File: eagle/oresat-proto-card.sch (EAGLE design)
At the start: 61 parts, among them J1 J-SAMTEC-TFM-110-X1-XXX-D-RA, J2 U.FL, J3 U.FL, J4 U.FL, J6 J-SAMTEC-TFM-120-X1-XXX-D-RA, J7 1.27MM-SWD-CONNECTOR, U1 TPS63070, U2 TCAN330, U6 STM32F042K6, X1 16MHZ-2.5x2mm

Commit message: Added some attributes.
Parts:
- J1: DIS (none) -> Digi-Key; DPN (none) -> SAM10113-ND; MFR (none) -> Samtec; MPN (none) -> TFM-110-01-L-D-RA
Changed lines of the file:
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@@
 <part name="JP8" library="pinhead" library_urn="urn:adsk.eagle:library:325" deviceset="PINHD-1X2" device="" package3d_urn="urn:adsk.eagle:package:22435/2"/>
 <part name="VBUS2" library="oresat-supplies" deviceset="VBUS" device=""/>
-<part name="J1" library="J-Samtec-TFM-110-X1-XXX-D-RA" deviceset="J-SAMTEC-TFM-110-X1-XXX-D-RA" device=""/>
+<part name="J1" library="J-Samtec-TFM-110-X1-XXX-D-RA" deviceset="J-SAMTEC-TFM-110-X1-XXX-D-RA" device="">
+<attribute name="DIS" value="Digi-Key"/>
+<attribute name="DPN" value="SAM10113-ND"/>
+<attribute name="MFR" value="Samtec"/>
+<attribute name="MPN" value="TFM-110-01-L-D-RA "/>
+</part>
 <part name="JP9" library="pinhead" library_urn="urn:adsk.eagle:library:325" deviceset="PINHD-1X10" device="" package3d_urn="urn:adsk.eagle:package:22406/2"/>
 <part name="JP10" library="pinhead" library_urn="urn:adsk.eagle:library:325" deviceset="PINHD-2X5" device="" package3d_urn="urn:adsk.eagle:package:22470/2"/>
@@
 <attribute name="NAME" x="22.86" y="83.185" size="1.778" layer="95" rot="MR0"/>
 <attribute name="VALUE" x="10.16" y="25.4" size="1.778" layer="96"/>
+<attribute name="DIS" x="16.51" y="57.15" size="1.778" layer="96" rot="MR0" display="off"/>
+<attribute name="DPN" x="16.51" y="57.15" size="1.778" layer="96" rot="MR0" display="off"/>
+<attribute name="MFR" x="16.51" y="57.15" size="1.778" layer="96" rot="MR0" display="off"/>
+<attribute name="MPN" x="16.51" y="57.15" size="1.778" layer="96" rot="MR0" display="off"/>
 </instance>
 <instance part="JP9" gate="A" x="64.77" y="57.15"/>

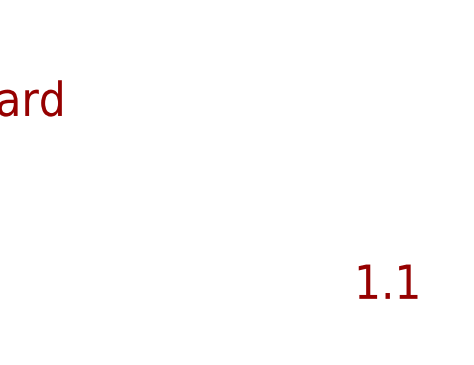
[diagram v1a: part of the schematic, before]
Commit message: Cleaned up ERC, changed VBAT to VBUS label.
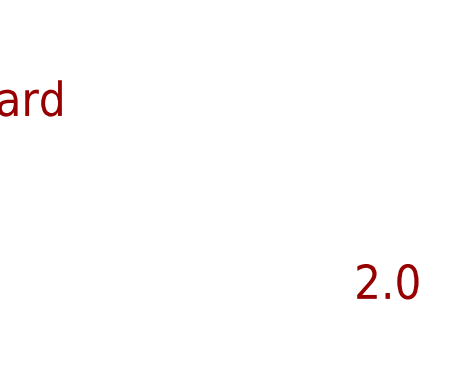
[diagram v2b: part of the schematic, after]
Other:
- note added: "2.0"
- note removed: "1.1"
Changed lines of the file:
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@@
 built in</text>
 <text x="341.63" y="26.67" size="3.81" layer="94">OreSat Proto-Card</text>
-<text x="416.56" y="6.35" size="3.81" layer="94">1.1</text>
+<text x="416.56" y="6.35" size="3.81" layer="94">2.0</text>
 <text x="11.43" y="5.08" size="1.778" layer="97">All resistors 0402 +/- 1% unless marked</text>
 <text x="11.43" y="2.54" size="1.778" layer="97">All caps are ceramic 10% X5R &gt;= 16V Vwv unless marked</text>

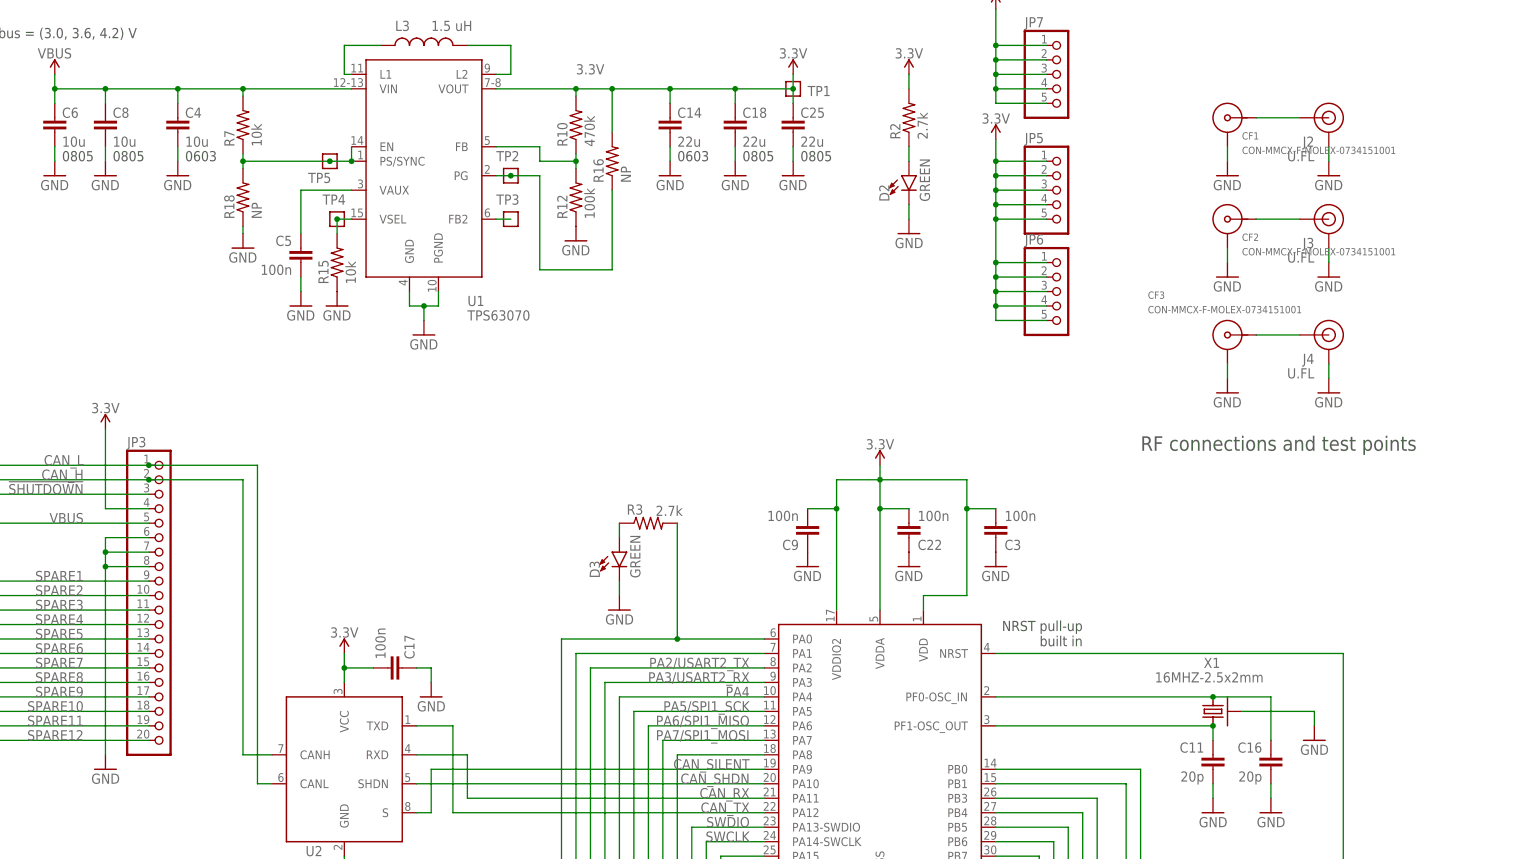
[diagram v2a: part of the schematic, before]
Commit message: Changes for the OreSat Backplane v1.0! Now with 100% more SMPM connectors.
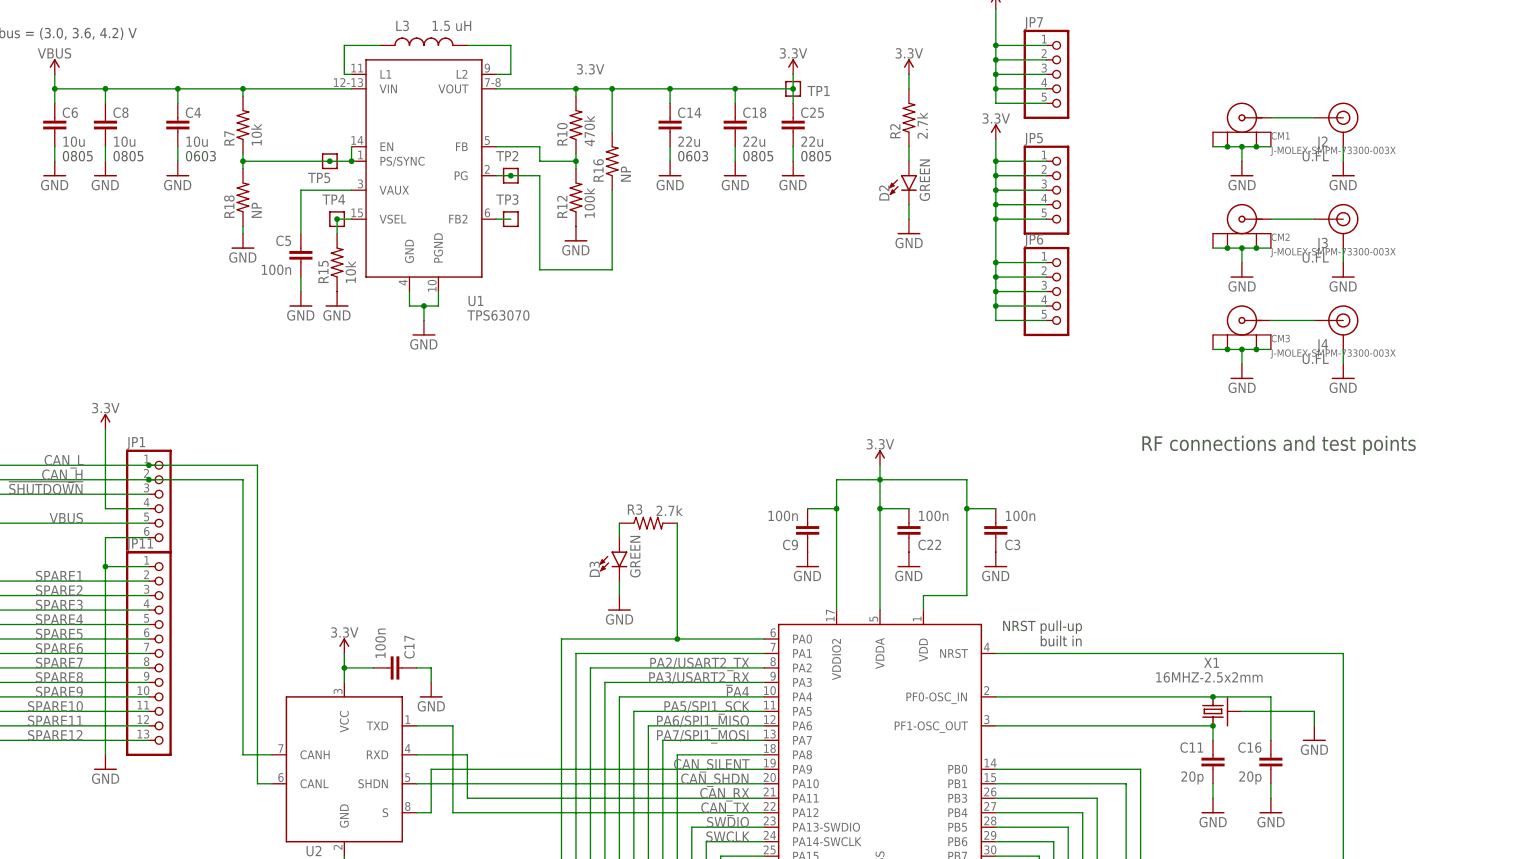
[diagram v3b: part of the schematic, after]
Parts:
- removed CF1, CF2, CF3: CON-MMCX-F-MOLEX-0734151001, oresat-eagle:CON-MMCX-F-MOLEX-0734151001
- removed JP3: (no value), pinhead:PINHD-1X20
- added CM1, CM2, CM3: J-MOLEX-SMPM-73300-003X, J-Molex-SMPM-73300-003X:J-MOLEX-SMPM-73300-003X
- added JP1: (no value), pinhead:PINHD-1X6
- added JP11: (no value), pinhead:PINHD-1X13
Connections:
- removed net N$2: CF2.CENTER, J3.SIGNAL
- removed net N$299: CF1.CENTER, J2.SIGNAL
- new net RF1: CM1.CENTER, J2.SIGNAL
- new net RF2: CM2.CENTER, J3.SIGNAL
- net !SHUTDOWN: now also JP1.3; no longer JP3.3
- net 3.3V: now also JP1.4; no longer JP3.4
- net CAN_H: now also JP1.2; no longer JP3.2
- net CAN_L: now also JP1.1; no longer JP3.1
- net GND: now also CM1.SHIELD, CM1.SHIELD1, CM1.SHIELD2, CM1.SHIELD3, CM2.SHIELD, CM2.SHIELD1, CM2.SHIELD2, CM2.SHIELD3, CM3.SHIELD, CM3.SHIELD1, CM3.SHIELD2, CM3.SHIELD3, JP1.6, JP11.1; no longer CF1.SHIELD, CF2.SHIELD, CF3.SHIELD, JP3.6, JP3.7, JP3.8
- net N$300: now also CM3.CENTER; no longer CF3.CENTER
- net SPARE1: now also JP11.2; no longer JP3.9
- net SPARE10: now also JP11.11; no longer JP3.18
- net SPARE11: now also JP11.12; no longer JP3.19
- net SPARE12: now also JP11.13; no longer JP3.20
- net SPARE2: now also JP11.3; no longer JP3.10
- net SPARE3: now also JP11.4; no longer JP3.11
- net SPARE4: now also JP11.5; no longer JP3.12
- net SPARE5: now also JP11.6; no longer JP3.13
- net SPARE6: now also JP11.7; no longer JP3.14
- net SPARE7: now also JP11.8; no longer JP3.15
- net SPARE8: now also JP11.9; no longer JP3.16
- net SPARE9: now also JP11.10; no longer JP3.17
- net VBUS: now also JP1.5; no longer JP3.5
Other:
- moved on the sheet: J2, J3, J4

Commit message: v3 protocard. Works with current 2018/11/22 structure.
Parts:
- removed JP2: (no value), pinhead:PINHD-1X12
- added JP3: (no value), pinhead:PINHD-1X3
- JP11: device pinhead:PINHD-1X13 -> pinhead:PINHD-2X6
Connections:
- net N$408 renamed AUX_CAN2_H
- net N$409 renamed AUX_CAN2_L
- net N$410 renamed AUX_VBUS2
- net N$411 renamed AUX_VBUS1
- net N$413 renamed AUX_GND3
- net N$414 renamed AUX_GND2
- net N$415 renamed AUX_CAN1_H
- net N$417 renamed AUX_CAN1_L
- net N$419 renamed AUX_GND1
- net N$421 renamed AUX_!SHUTDOWN
- removed net CAN_H: J6.3, J6.4, JP1.2, JP10.3, JP10.4, U2.CANH
- removed net CAN_L: J6.1, J6.2, JP1.1, JP10.1, JP10.2, U2.CANL
- removed net SPARE11: J6.37, J6.38, JP11.12, JP2.11
- removed net SPARE12: J6.39, J6.40, JP11.13, JP2.12
- new net CAN1_H: J6.33, J6.34, JP1.1, JP10.5, JP10.6, U2.CANH
- new net CAN1_L: J6.35, J6.36, JP1.2, JP10.7, JP10.8, U2.CANL
- new net CAN2_H: J6.23, J6.24, JP11.12
- new net CAN2_L: J6.21, J6.22, JP11.11
- net !SHUTDOWN: now also J6.39, J6.40, JP10.10, JP10.9; no longer J6.7, J6.8, JP10.5, JP10.6
- net GND: now also J6.29, J6.30, J6.31, J6.32, J6.37, J6.38; no longer J6.10, J6.11, J6.12, J6.5, J6.6, J6.9, JP11.1
- net SPARE1: now also J6.19, J6.20, JP11.10; no longer J6.17, J6.18, JP11.2, JP2.1
- net SPARE10: now also J6.1, J6.2, JP11.2; no longer J6.35, J6.36, JP11.11, JP2.10
- net SPARE2: now also J6.17, J6.18, JP11.9; no longer J6.19, J6.20, JP11.3, JP2.2
- net SPARE3: now also J6.15, J6.16, JP11.7; no longer J6.21, J6.22, JP11.4, JP2.3
- net SPARE4: now also J6.13, J6.14, JP11.8; no longer J6.23, J6.24, JP11.5, JP2.4
- net SPARE5: now also J6.11, J6.12, JP11.5; no longer J6.25, J6.26, JP11.6, JP2.5
- net SPARE6: now also J6.10, J6.9, JP11.6; no longer J6.27, J6.28, JP11.7, JP2.6
- net SPARE7: now also J6.7, J6.8, JP11.3; no longer J6.29, J6.30, JP11.8, JP2.7
- net SPARE8: now also J6.5, J6.6, JP11.4; no longer J6.31, J6.32, JP11.9, JP2.8
- net SPARE9: now also J6.3, J6.4, JP11.1; no longer J6.33, J6.34, JP11.10, JP2.9
- net VBUS: now also J6.25, J6.26, J6.27, J6.28, JP10.1, JP10.2, JP10.3, JP10.4, JP3.1, JP3.2, JP3.3; no longer J6.13, J6.14, J6.15, J6.16, JP10.10, JP10.7, JP10.8, JP10.9
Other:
- moved on the sheet: CM1, CM2, CM3, J2, J3, J4, JP1, JP10, JP5, JP6, JP7, JP9

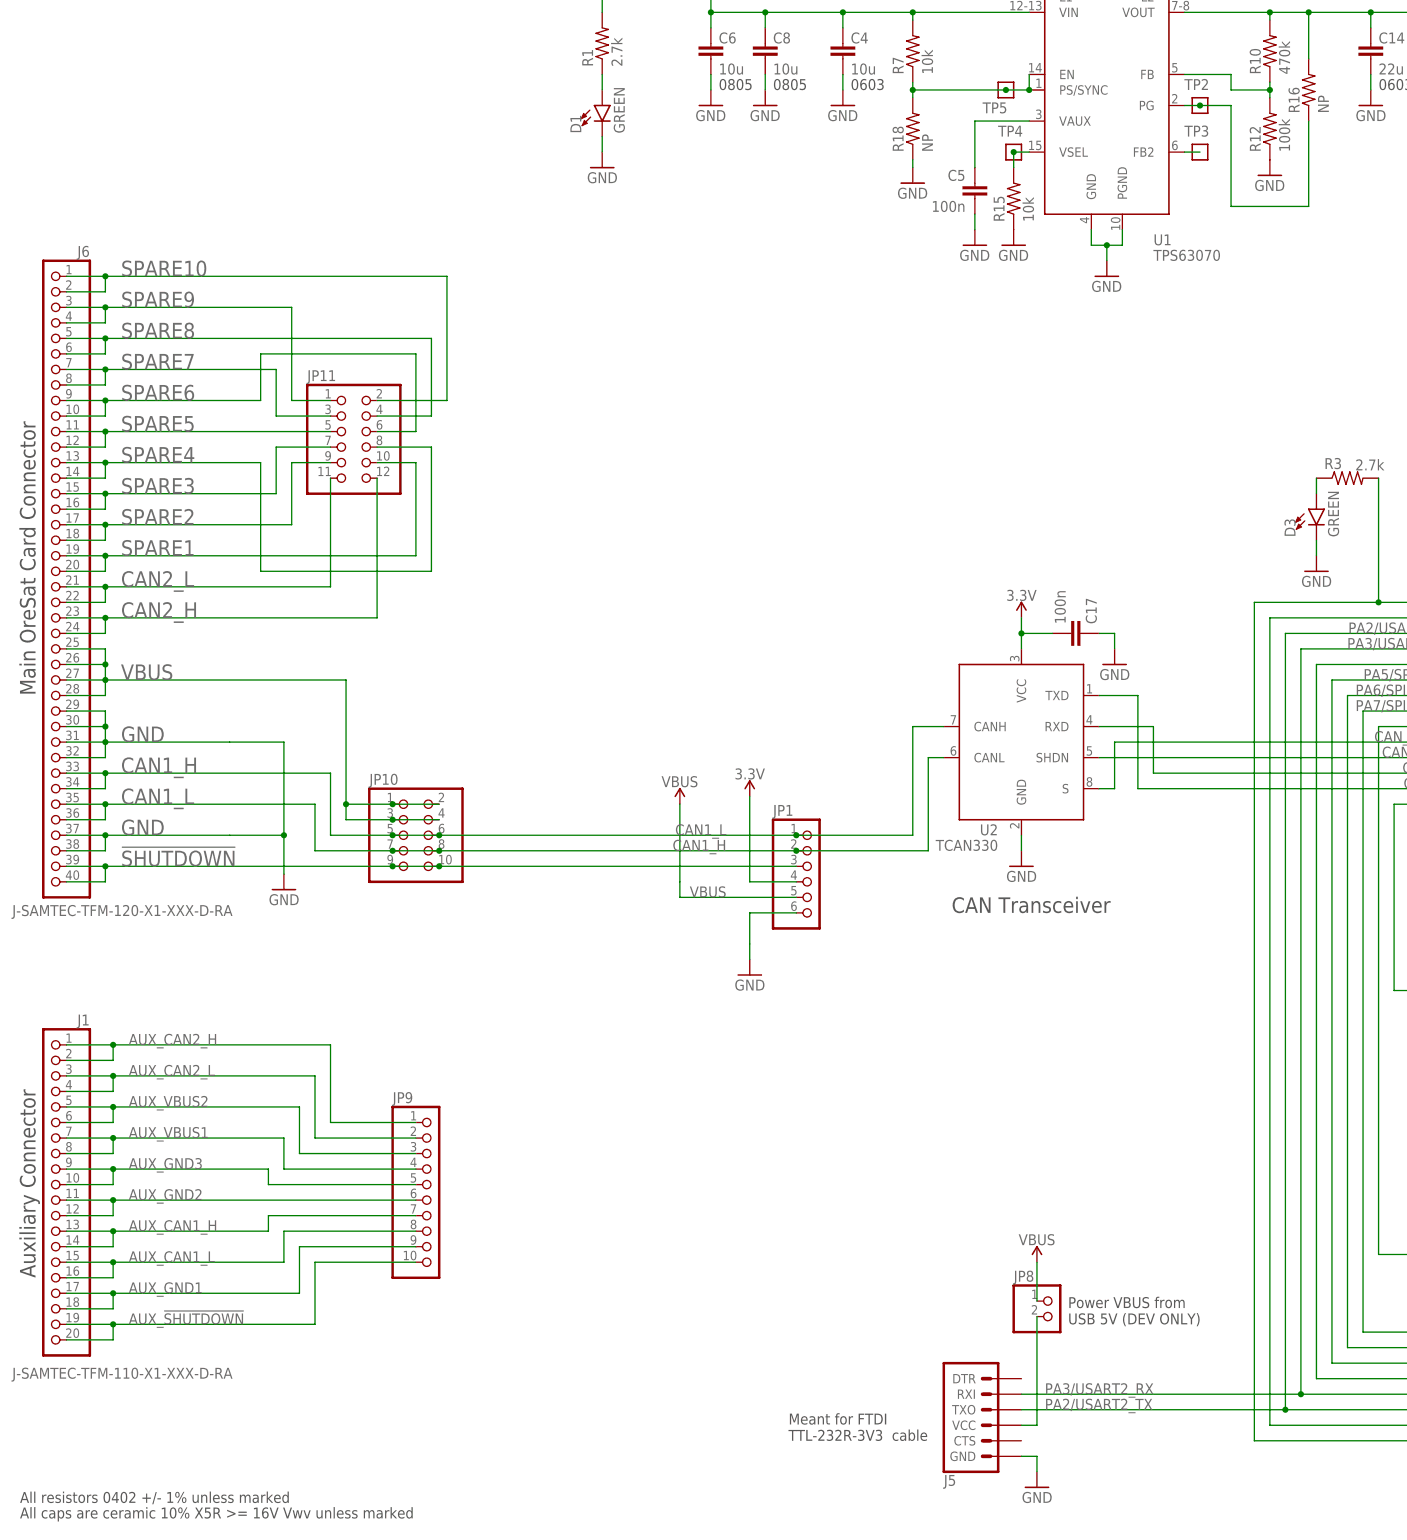
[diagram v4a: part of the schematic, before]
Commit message: minor tweaks, including fixing power supply resistors.
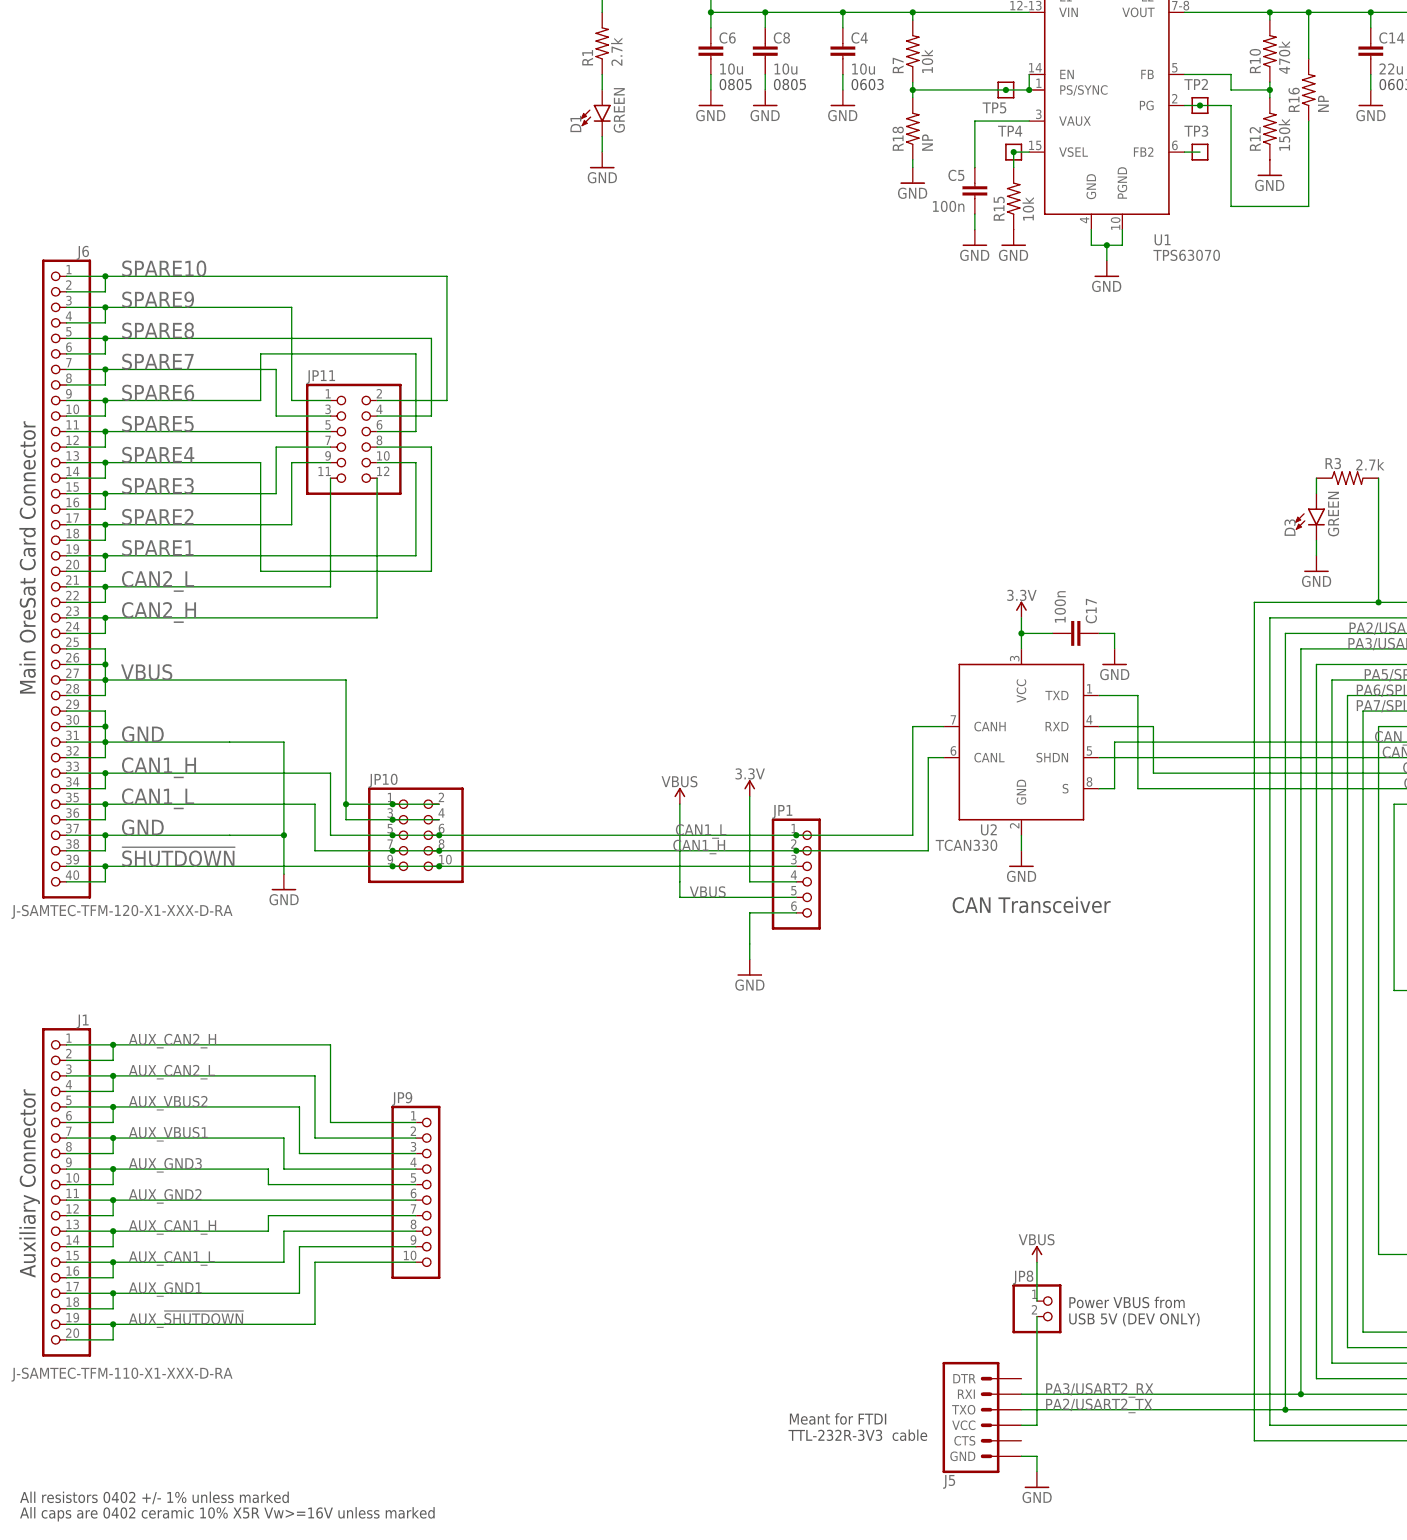
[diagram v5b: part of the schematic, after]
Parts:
- R12: value 100k -> 150k
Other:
- note added: "All caps are 0402 ceramic 10% X5R Vw>=16V unless marked"
- note removed: "All caps are ceramic 10% X5R >= 16V Vwv unless marked"
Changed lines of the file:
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@@
 <setting verticaltext="up"/>
 </settings>
-<grid distance="0.05" unitdist="inch" unit="inch" style="lines" multiple="2" display="no" altdistance="0.01" altunitdist="inch" altunit="inch"/>
+<grid distance="0.1" unitdist="inch" unit="inch" style="lines" multiple="1" display="no" altdistance="0.01" altunitdist="inch" altunit="inch"/>
 <layers>
 <layer number="1" name="Top" color="4" fill="1" visible="no" active="no"/>
@@
 <attribute name="MPN" value="RC1005F6653CS"/>
 </part>
-<part name="R12" library="rcl_custom" deviceset="R-US_" device="0402-B-NOSILK" value="100k">
+<part name="R12" library="rcl_custom" deviceset="R-US_" device="0402-B-NOSILK" value="150k">
 <attribute name="DIS" value="Digi-Key"/>
 <attribute name="DPN" value="1276-4275-1-ND"/>
@@
 <text x="416.56" y="6.35" size="3.81" layer="94">2.0</text>
 <text x="11.43" y="5.08" size="1.778" layer="97">All resistors 0402 +/- 1% unless marked</text>
-<text x="11.43" y="2.54" size="1.778" layer="97">All caps are ceramic 10% X5R &gt;= 16V Vwv unless marked</text>
+<text x="11.43" y="2.54" size="1.778" layer="97">All caps are 0402 ceramic 10% X5R Vw&gt;=16V unless marked</text>
 <text x="147.32" y="236.22" size="1.778" layer="97">0603</text>
 <text x="125.73" y="236.22" size="1.778" layer="97">0805</text>
